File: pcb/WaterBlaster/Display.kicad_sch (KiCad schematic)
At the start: 6 parts, among them J16 430450800

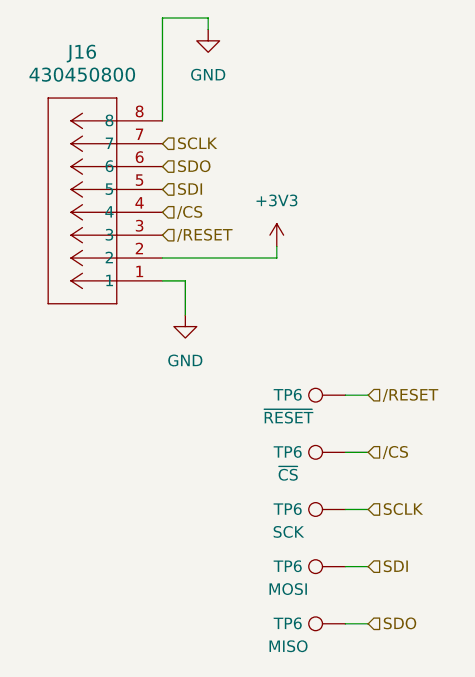
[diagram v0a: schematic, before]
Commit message: Updating firmware and CAD
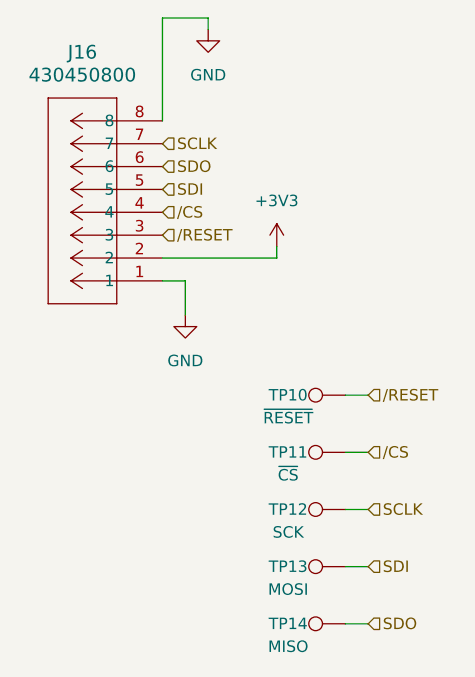
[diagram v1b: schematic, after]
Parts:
- renumbered TP6 to TP10, TP6 to TP11, TP6 to TP12, TP6 to TP13, TP6 to TP14
